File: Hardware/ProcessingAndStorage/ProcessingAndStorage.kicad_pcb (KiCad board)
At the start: 2 copper layers, 85 x 60 mm, 31 parts, among them J1 Micro_SD_Card_Det2, J5 Conn_02x11_Odd_Even, SW2 SW_SPDT_XKB_DMx-xxxx-1, U1 LD1117S50TR_SOT223, U2 ESP-12E, U3 LD1117S50TR_SOT223

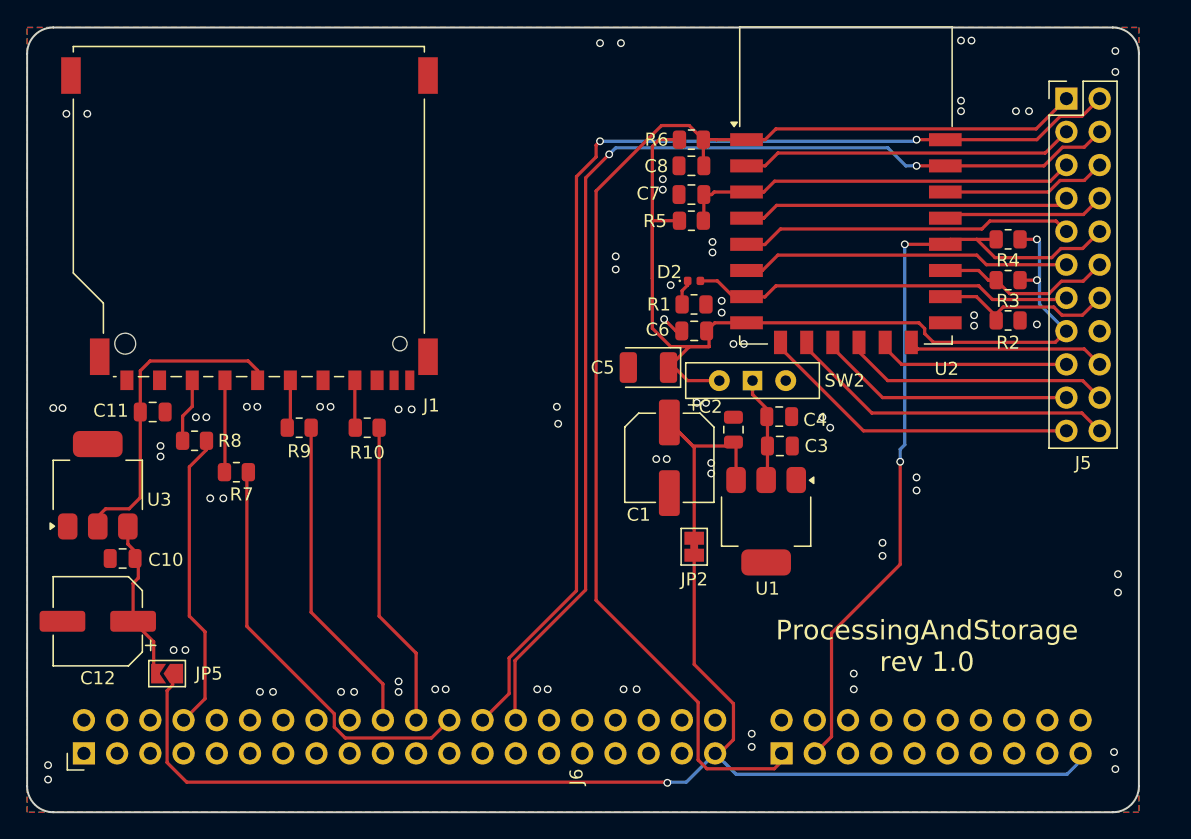
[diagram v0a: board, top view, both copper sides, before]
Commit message: make boards smaller, fix sd card slot
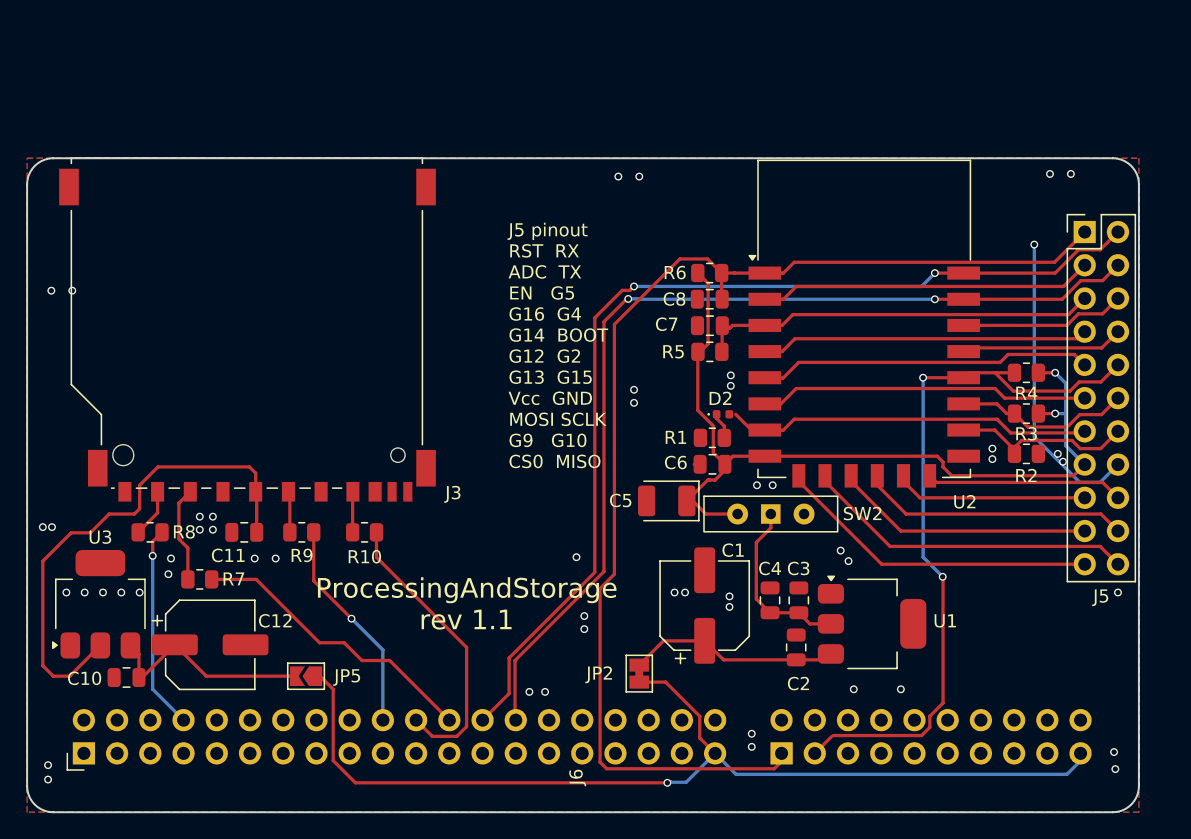
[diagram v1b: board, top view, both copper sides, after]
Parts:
- removed J1: Micro_SD_Card_Det2, Connector_Card:SD_TE_2041021
- added J3: SD_Card_Receptacle, Connector_Card:SD_TE_2041021, F.Cu at (146.8, 83.5)
- moved C2 17.3 mm to (188.8, 107.4)
- moved C4 14.1 mm to (186.8, 103.8), turned to 90 degrees
- moved C3 11.9 mm to (189.0, 103.8), turned to 90 degrees
- moved C1 11.6 mm to (181.8, 104.2), turned to 90 degrees
- moved C11 11.6 mm to (146.6, 98.6), turned to 180 degrees
- moved U1 11.3 mm to (194.6, 105.6), turned to 0 degrees
- moved JP5 10.6 mm to (151.3, 109.6)
- moved JP2 10.6 mm to (176.8, 109.4)
- moved D2 10.4 mm to (183.2, 89.6)
- moved C5 10.3 mm to (178.9, 96.2)
- moved C6 10.3 mm to (182.4, 93.4)
- moved C8 10.3 mm to (182.2, 80.8)
- moved J5 10.3 mm to (210.9, 75.6)
- moved R1 10.3 mm to (182.4, 91.4), turned to 180 degrees
- moved R3 10.3 mm to (206.4, 89.5)
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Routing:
- net GND: track 1.72 -> 23.6 mm, vias 79 -> 52
- net 5V: track 96.0 -> 76.1 mm
- net Net-(J3-VDD): track 23.9 -> 38.7 mm
- net USART1_TX: track 85.5 -> 74.3 mm
- net ESP_PWR: track 75.6 -> 64.6 mm
- net USART1_RX: track 87.5 -> 77.0 mm
- net SPI1_MOSI: track 31.8 -> 22.6 mm
- net SPI1_SCK: track 24.6 -> 16.6 mm, vias 0 -> 1
- net GPIO_9: track 23.1 -> 15.6 mm, vias 0 -> 1
- net 3V3: track 6.60 -> 13.4 mm
- net NRST: track 95.4 -> 90.0 mm
- net Net-(JP5-B): track 11.5 -> 16.5 mm
- net BOOT0: track 59.7 -> 55.1 mm
- net Net-(JP2-B): track 17.7 -> 15.6 mm
- net /WiFi/GPIO13: track 28.1 -> 26.8 mm
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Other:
- board size 85 x 60 mm -> 85 x 50 mm
- board text added: "J5 pinout RST RX ADC TX EN G5 G16 G4 G14 BOOT G12 G2 G13 G15 Vcc GND MOSI SCLK G9 G10 CS0 MISO"
- board text added: "ProcessingAndStorage rev 1.1"
- board text removed: "ProcessingAndStorage rev 1.0"

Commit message: make hw
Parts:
- removed J5: Conn_02x11_Odd_Even, Connector_PinHeader_2.54mm:PinHeader_2x11_P2.54mm_Vertical
- removed SW2: SW_SPDT_XKB_DMx-xxxx-1, Button_Switch_THT:SW_Slide-03_Wuerth-WS-SLTV_10x2.5x6.4_P2.54mm
- added C13: 330n, Capacitor_SMD:C_0805_2012Metric, F.Cu at (139.4, 99.2)
- added C18: 100n, Capacitor_SMD:C_0805_2012Metric, F.Cu at (177.2, 75.5)
- added C20: 100n, Capacitor_SMD:C_0805_2012Metric, F.Cu at (177.2, 72.0)
- added C9: 10u, Capacitor_SMD:C_0805_2012Metric, F.Cu at (175.1, 72.0)
- added D1: LED, LED_SMD:LED_0402_1005Metric, F.Cu at (199.2, 71.1)
- added D3: LED, LED_SMD:LED_0402_1005Metric, F.Cu at (213.6, 109.6)
- added D4: LED, LED_SMD:LED_0402_1005Metric, F.Cu at (201.4, 71.1)
- added J1: USB_B_Micro, Connector_USB:USB_Micro-B_Molex-105017-0001, F.Cu at (211.6, 103.0)
- added J2: Conn_02x10_Odd_Even, Connector_PinHeader_2.54mm:PinHeader_2x10_P2.54mm_Horizontal, F.Cu at (204.3, 72.9)
- added JP1: SolderJumper_2_Bridged, Jumper:SolderJumper-2_P1.3mm_Bridged_Pad1.0x1.5mm, F.Cu at (182.0, 91.1)
- added JP3: SolderJumper_2_Bridged, Jumper:SolderJumper-2_P1.3mm_Bridged_Pad1.0x1.5mm, F.Cu at (199.8, 82.2)
- added Q1: BC846, Package_TO_SOT_SMD:SOT-23, F.Cu at (197.4, 103.4)
- added Q2: BC846, Package_TO_SOT_SMD:SOT-23, F.Cu at (201.1, 103.4)
- added Q3: BC846, Package_TO_SOT_SMD:SOT-23, F.Cu at (191.8, 103.4)
- added Q4: BC846, Package_TO_SOT_SMD:SOT-23, F.Cu at (186.2, 103.4)
- added R11: 1k, Resistor_SMD:R_0805_2012Metric, F.Cu at (201.4, 73.9)
- added R17: 10k, Resistor_SMD:R_0805_2012Metric, F.Cu at (199.3, 108.5)
- added R18: 10k, Resistor_SMD:R_0805_2012Metric, F.Cu at (199.3, 106.4)
- added R20: 10k, Resistor_SMD:R_0805_2012Metric, F.Cu at (175.1, 75.5)
- added TP1: TestPoint, TestPoint:TestPoint_Pad_D1.5mm, F.Cu at (199.1, 91.1)
- added TP2: TestPoint, TestPoint:TestPoint_Pad_D1.5mm, F.Cu at (195.0, 94.7)
- added TP3: TestPoint, TestPoint:TestPoint_Pad_D1.5mm, F.Cu at (196.7, 92.6)
- added TP4: TestPoint, TestPoint:TestPoint_Pad_D1.5mm, F.Cu at (190.5, 97.8)
- added U4: ESP32-WROOM-32E, RF_Module:ESP32-WROOM-32D, F.Cu at (188.3, 79.1)
- C5: value 47u/6V3 -> 100n; footprint Capacitor_Tantalum_SMD:CP_EIA-3528-21_Kemet-B -> Capacitor_SMD:C_0805_2012Metric
- C7: value 100n -> 10u
- C8: value 470p -> 10u
- R1: value 470R -> 10k
- R2, R3, R6: value 10k -> 1k
- U1, U3: footprint Package_TO_SOT_SMD:SOT-223 -> Package_TO_SOT_SMD:SOT-223-3_TabPin2
- U2: value ESP-12E -> CH340X; footprint RF_Module:ESP-12E -> Package_SO:MSOP-10_3x3mm_P0.5mm
- moved D2 35.8 mm to (213.6, 108.5)
- moved C7 34.2 mm to (203.5, 109.5), turned to -90 degrees
- moved R1 32.9 mm to (209.8, 109.5), turned to 90 degrees
- moved C5 31.7 mm to (207.7, 109.5), turned to -90 degrees
- moved C6 28.2 mm to (205.6, 109.5), turned to -90 degrees
- moved R3 26.1 mm to (186.8, 106.7)
- moved U2 24.9 mm to (205.3, 104.5), turned to -90 degrees
- moved U1 24.6 mm to (171.0, 98.8), turned to 90 degrees
- moved R4 20.9 mm to (194.6, 103.7), turned to 90 degrees
- moved R2 20.2 mm to (192.0, 106.7), turned to 180 degrees
- moved R5 20.1 mm to (189.0, 103.7), turned to 90 degrees
- moved R6 17.7 mm to (199.2, 73.9), turned to -90 degrees
- moved JP5 15.1 mm to (136.2, 109.8), turned to 0 degrees
- moved C3 14.9 mm to (175.8, 96.8), turned to -90 degrees
- moved C2 14.3 mm to (175.8, 101.4)
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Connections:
- C3 pad 1: 3V3 -> ESP_3V3
- C4 pad 1: 3V3 -> ESP_3V3
- C5 pad 1: ESP_PWR -> Net-(U2-V3)
- C6 pad 1: ESP_PWR -> ESP_3V3
- C7 pad 1: /WiFi/EN -> ESP_3V3
- C8 pad 1: NRST -> ESP_3V3
- D2 pad 2: /WiFi/GPIO13 -> ESP_3V3
- J6 pad 41: NRST -> unconnected-(J6-Pin_41-Pad41)
- J6 pad 43: BOOT0 -> unconnected-(J6-Pin_43-Pad43)
- R1 pad 1: Net-(D2-K) -> GND
- R1 pad 2: GND -> Net-(J1-VBUS)
- R2 pad 1: /WiFi/GPIO15 -> Net-(D2-K)
- R2 pad 2: GND -> Net-(Q3-C)
- R3 pad 1: ESP_PWR -> Net-(D3-K)
- R3 pad 2: /WiFi/GPIO2 -> Net-(Q4-C)
- R4 pad 1: ESP_PWR -> Net-(Q1-E)
- R4 pad 2: BOOT0 -> Net-(Q3-B)
- R5 pad 1: ESP_PWR -> Net-(Q2-E)
- R5 pad 2: /WiFi/EN -> Net-(Q4-B)
- R6 pad 1: ESP_PWR -> Net-(D1-K)
- R6 pad 2: NRST -> GND
- U1 pad 2: 3V3 -> ESP_3V3
- U2 pad 1: NRST -> /SerialProgrammer/USB+
- U2 pad 10: /WiFi/ESP32_MISO -> Net-(U2-V3)
- U2 pad 2: /WiFi/ESP_ADC -> /SerialProgrammer/USB-
- U2 pad 3: /WiFi/EN -> GND
- U2 pad 4: /WiFi/GPIO16 -> Net-(Q1-E)
- U2 pad 5: /WiFi/GPIO14 -> unconnected-(U2-~{CTS}-Pad5)
- U2 pad 6: /WiFi/GPIO12 -> Net-(Q2-E)
- U2 pad 7: /WiFi/GPIO13 -> ESP_3V3
- U2 pad 8: ESP_PWR -> ESP_U0_TX
- U2 pad 9: /WiFi/ESP32_CS0 -> ESP_U0_RX
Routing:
- net ESP_3V3: track 0.00 -> 151.7 mm, vias 0 -> 1
- net NRST: track 90.0 -> 0.00 mm
- net ESP_PWR: track 64.6 -> 0.00 mm, vias 2 -> 0
- net BOOT0: track 55.1 -> 0.00 mm, vias 2 -> 0
- net ESP_EN: track 0.00 -> 45.5 mm
- net ESP_U0_TX: track 0.00 -> 41.5 mm, vias 0 -> 2
- net ESP_U0_RX: track 0.00 -> 39.0 mm
- net /WiFi/IO14: track 0.00 -> 32.7 mm, vias 0 -> 1
- net /WiFi/IO26: track 0.00 -> 31.0 mm, vias 0 -> 1
- net /WiFi/EN: track 30.6 -> 0.00 mm
- net /WiFi/IO33: track 0.00 -> 30.2 mm, vias 0 -> 1
- net /WiFi/IO35: track 0.00 -> 30.0 mm, vias 0 -> 1
- net /WiFi/SENSOR_VP: track 0.00 -> 28.7 mm, vias 0 -> 1
- net /WiFi/IO27: track 0.00 -> 28.7 mm, vias 0 -> 1
- net /WiFi/SENSOR_VN: track 0.00 -> 28.6 mm, vias 0 -> 1
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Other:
- board text added: "J2 pins 23 22 21 19 18 VP VN VCC 34 35 32 33 25 26 27 14 13 04 GN GN"
- board text added: "ProcessingAndStorage rev 1.2"
- board text removed: "J5 pinout RST RX ADC TX EN G5 G16 G4 G14 BOOT G12 G2 G13 G15 Vcc GND MOSI SCLK G9 G10 CS0 MISO"
- board text removed: "ProcessingAndStorage rev 1.1"

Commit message: xx
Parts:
- J1: footprint Connector_USB:USB_Micro-B_Molex-105017-0001 -> HardwareDataLogger:USB_Micro-B_Molex-105017-0001_Extra_Mechanical_Pads
- moved J1 1.66 mm to (210.0, 102.7)
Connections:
- net /SerialProgrammer/USB+ renamed /SerialProgrammer/USB_P
- net /SerialProgrammer/USB- renamed /SerialProgrammer/USB_N
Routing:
- net /WiFi/IO22: track 19.2 -> 14.1 mm
- net /WiFi/IO23: track 11.8 -> 8.86 mm
- net /SerialProgrammer/USB_P: track 4.21 -> 6.01 mm
- net Net-(J1-VBUS): track 5.15 -> 6.53 mm
- net ESP_3V3: track 151.7 -> 153.0 mm
- net /SerialProgrammer/USB_N: track 5.37 -> 6.37 mm
- net ESP_U0_TX: track 41.5 -> 40.5 mm
- net GND: track 7.46 -> 7.49 mm, vias 48 -> 51
